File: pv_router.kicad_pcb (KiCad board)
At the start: 4 copper layers, 75 x 69.2 mm, 50 parts, among them IC1 L6981C33DR, IC2 ATM90E26-YU-B, IC3 ESP32-C3-WROOM-02-N4, J1 Barrel_Jack_Switch_Pin3Ring, J2 AudioJack3, J3 AudioJack3, J4 Barrel_Jack_Switch_Pin3Ring, J5 UART, J6 ToSSR, Q1 BSS138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

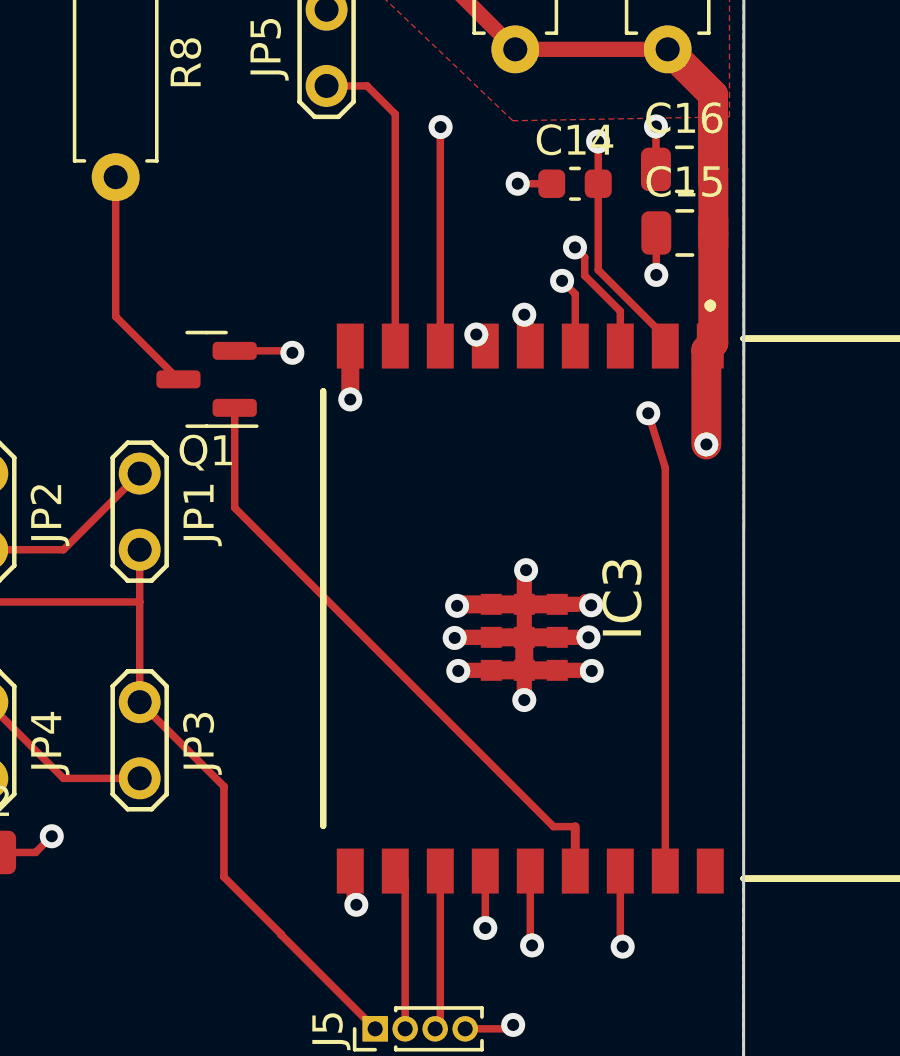
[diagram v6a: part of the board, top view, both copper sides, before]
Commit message: PCB: fix spaces between some tracks
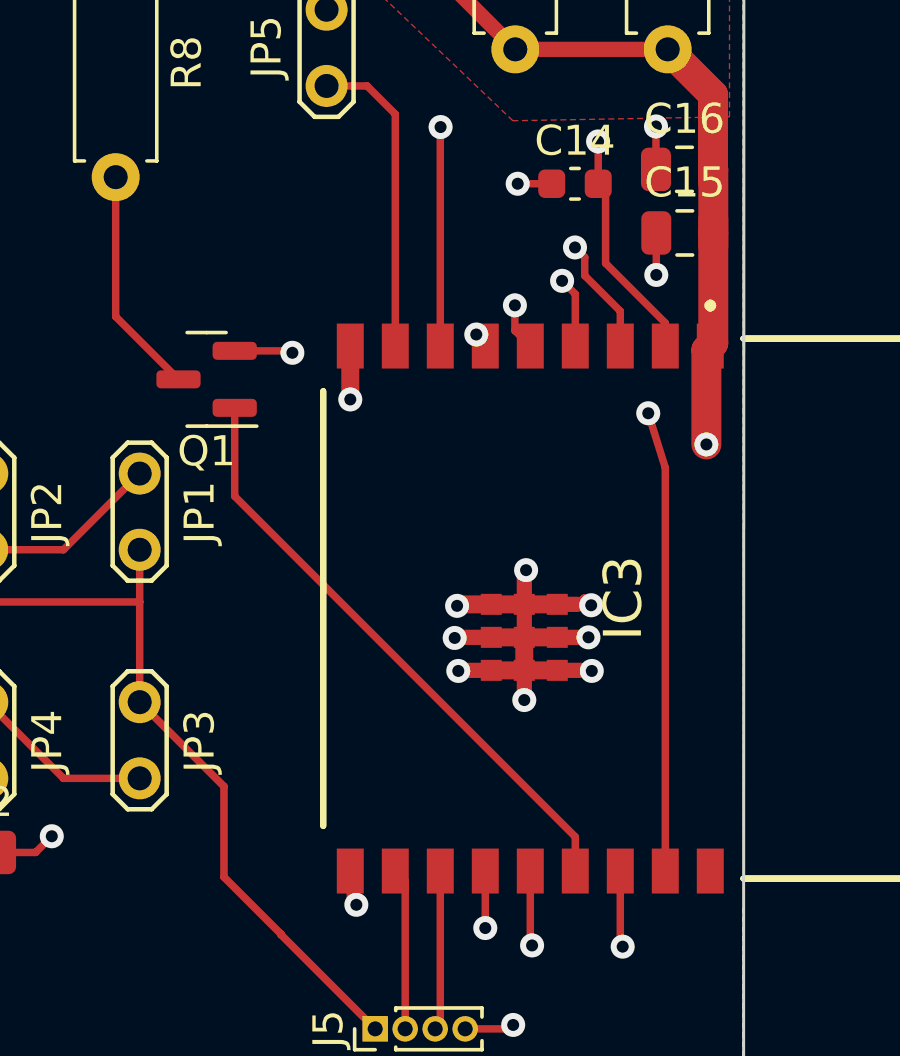
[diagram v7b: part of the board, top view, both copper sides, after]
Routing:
- net /adc/CF2: track 40.6 -> 41.4 mm
- net /adc/CF1: track 43.9 -> 44.5 mm
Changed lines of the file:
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@@
   (segment (start 164.07 140.71) (end 159.38 140.71) (width 0.25) (layer "F.Cu") (net 11))
   (segment (start 165.66 137.0321) (end 165.913264 137.285364) (width 0.3) (layer "F.Cu") (net 11))
-  (segment (start 195.155 121.555) (end 197.39 123.79) (width 0.25) (layer "F.Cu") (net 12))
-  (segment (start 195.155 118.68) (end 195.155 121.555) (width 0.25) (layer "F.Cu") (net 12))
+  (segment (start 195.4 121.33) (end 197.39 123.32) (width 0.25) (layer "F.Cu") (net 12))
   (segment (start 191.91 99.3) (end 193.12 99.3) (width 0.25) (layer "F.Cu") (net 12))
-  (segment (start 197.39 123.79) (end 197.39 124.09) (width 0.25) (layer "F.Cu") (net 12))
+  (segment (start 197.39 123.32) (end 197.39 124.09) (width 0.25) (layer "F.Cu") (net 12))
+  (segment (start 195.4 118.925) (end 195.4 121.33) (width 0.25) (layer "F.Cu") (net 12))
   (segment (start 185.11 99.3) (end 191.91 99.3) (width 0.25) (layer "F.Cu") (net 12))
   (segment (start 193.12 99.3) (end 197.48 103.66) (width 0.25) (layer "F.Cu") (net 12))
+  (segment (start 195.155 118.68) (end 195.4 118.925) (width 0.25) (layer "F.Cu") (net 12))
   (segment (start 197.48 106.57) (end 197.47 106.58) (width 0.25) (layer "F.Cu") (net 12))
   (segment (start 195.155 118.68) (end 195.155 117.275) (width 0.25) (layer "F.Cu") (net 12))
@@
   (via (at 191.09 123.705) (size 0.8) (drill 0.4) (layers "F.Cu" "B.Cu") (net 19))
   (via (at 169.01 132.35) (size 0.8) (drill 0.4) (layers "F.Cu" "B.Cu") (net 19))
-  (segment (start 169.01 132.09) (end 177.56 123.54) (width 0.25) (layer "In2.Cu") (net 19))
+  (segment (start 190.945 123.56) (end 191.09 123.705) (width 0.25) (layer "In2.Cu") (net 19))
+  (segment (start 169.01 132.09) (end 177.54 123.56) (width 0.25) (layer "In2.Cu") (net 19))
+  (segment (start 177.54 123.56) (end 190.945 123.56) (width 0.25) (layer "In2.Cu") (net 19))
   (segment (start 169.01 132.35) (end 169.01 132.09) (width 0.25) (layer "In2.Cu") (net 19))
-  (segment (start 177.56 123.54) (end 190.925 123.54) (width 0.25) (layer "In2.Cu") (net 19))
-  (segment (start 190.925 123.54) (end 191.09 123.705) (width 0.25) (layer "In2.Cu") (net 19))
-  (segment (start 192.89 123.245) (end 192.69 123.045) (width 0.25) (layer "F.Cu") (net 20))
+  (segment (start 192.3775 123.5775) (end 192.3775 122.7325) (width 0.25) (layer "F.Cu") (net 20))
   (segment (start 167.61 135.96) (end 167.61 134.400756) (width 0.25) (layer "F.Cu") (net 20))
-  (segment (start 192.89 124.09) (end 192.89 123.245) (width 0.25) (layer "F.Cu") (net 20))
+  (segment (start 192.89 124.09) (end 192.3775 123.5775) (width 0.25) (layer "F.Cu") (net 20))
   (segment (start 167.61 134.400756) (end 167.091412 133.882168) (width 0.25) (layer "F.Cu") (net 20))
-  (via (at 192.69 123.045) (size 0.8) (drill 0.4) (layers "F.Cu" "B.Cu") (net 20))
+  (via (at 192.3775 122.7325) (size 0.8) (drill 0.4) (layers "F.Cu" "B.Cu") (net 20))
   (via (at 167.091412 133.882168) (size 0.8) (drill 0.4) (layers "F.Cu" "B.Cu") (net 20))
-  (segment (start 167.091412 132.852309) (end 177.013721 122.93) (width 0.25) (layer "In2.Cu") (net 20))
+  (segment (start 177.211221 122.7325) (end 192.3775 122.7325) (width 0.25) (layer "In2.Cu") (net 20))
+  (segment (start 167.091412 132.852309) (end 177.211221 122.7325) (width 0.25) (layer "In2.Cu") (net 20))
   (segment (start 167.091412 133.882168) (end 167.091412 132.852309) (width 0.25) (layer "In2.Cu") (net 20))
-  (segment (start 192.575 122.93) (end 192.69 123.045) (width 0.25) (layer "In2.Cu") (net 20))
-  (segment (start 177.013721 122.93) (end 192.575 122.93) (width 0.25) (layer "In2.Cu") (net 20))
   (segment (start 186.89 142.512829) (end 187.092171 142.715) (width 0.25) (layer "F.Cu") (net 21))
   (segment (start 165.01 137.513471) (end 165.113264 137.616735) (width 0.25) (layer "F.Cu") (net 21))
@@
   (via (at 163.69995 133.64995) (size 0.8) (drill 0.4) (layers "F.Cu" "B.Cu") (net 23))
   (via (at 193.94999 121.916283) (size 0.8) (drill 0.4) (layers "F.Cu" "B.Cu") (net 23))
+  (segment (start 192.833707 120.8) (end 193.94999 121.916283) (width 0.25) (layer "In2.Cu") (net 23))
+  (segment (start 167.085 130.791016) (end 167.085 129.615) (width 0.25) (layer "In2.Cu") (net 23))
+  (segment (start 167.085 129.615) (end 175.9 120.8) (width 0.25) (layer "In2.Cu") (net 23))
+  (segment (start 163.69995 133.64995) (end 164.226066 133.64995) (width 0.25) (layer "In2.Cu") (net 23))
   (segment (start 164.226066 133.64995) (end 167.085 130.791016) (width 0.25) (layer "In2.Cu") (net 23))
-  (segment (start 175.225392 121.664888) (end 193.698595 121.664888) (width 0.25) (layer "In2.Cu") (net 23))
-  (segment (start 167.085 130.791016) (end 167.085 129.80528) (width 0.25) (layer "In2.Cu") (net 23))
-  (segment (start 167.085 129.80528) (end 175.225392 121.664888) (width 0.25) (layer "In2.Cu") (net 23))
-  (segment (start 163.69995 133.64995) (end 164.226066 133.64995) (width 0.25) (layer "In2.Cu") (net 23))
-  (segment (start 193.698595 121.664888) (end 193.94999 121.916283) (width 0.25) (layer "In2.Cu") (net 23))
+  (segment (start 175.9 120.8) (end 192.833707 120.8) (width 0.25) (layer "In2.Cu") (net 23))
   (segment (start 195.89 124.09) (end 195.89 122.926396) (width 0.25) (layer "F.Cu") (net 24))
   (segment (start 163.06 134.574858) (end 162.52001 134.034868) (width 0.25) (layer "F.Cu") (net 24))
@@
   (via (at 194.380046 120.80346) (size 0.8) (drill 0.4) (layers "F.Cu" "B.Cu") (net 24))
   (via (at 162.52001 134.034868) (size 0.8) (drill 0.4) (layers "F.Cu" "B.Cu") (net 24))
+  (segment (start 175.613984 120.07) (end 193.646586 120.07) (width 0.25) (layer "In2.Cu") (net 24))
+  (segment (start 162.52001 134.034868) (end 162.52001 133.733874) (width 0.25) (layer "In2.Cu") (net 24))
+  (segment (start 193.646586 120.07) (end 194.380046 120.80346) (width 0.25) (layer "In2.Cu") (net 24))
+  (segment (start 162.52001 133.733874) (end 165.535 130.718884) (width 0.25) (layer "In2.Cu") (net 24))
   (segment (start 165.535 130.718884) (end 165.535 130.148984) (width 0.25) (layer "In2.Cu") (net 24))
-  (segment (start 165.535 130.148984) (end 174.880524 120.80346) (width 0.25) (layer "In2.Cu") (net 24))
-  (segment (start 162.52001 133.733874) (end 165.535 130.718884) (width 0.25) (layer "In2.Cu") (net 24))
-  (segment (start 174.880524 120.80346) (end 194.380046 120.80346) (width 0.25) (layer "In2.Cu") (net 24))
-  (segment (start 162.52001 134.034868) (end 162.52001 133.733874) (width 0.25) (layer "In2.Cu") (net 24))
+  (segment (start 165.535 130.148984) (end 175.613984 120.07) (width 0.25) (layer "In2.Cu") (net 24))
   (segment (start 192.89 144.01) (end 192.89 141.59) (width 0.25) (layer "F.Cu") (net 25))
   (segment (start 162.41 136.94) (end 161.62 137.73) (width 0.25) (layer "F.Cu") (net 25))
@@
   (via (at 167.824357 131.023348) (size 0.8) (drill 0.4) (layers "F.Cu" "B.Cu") (net 26))
   (segment (start 167.824357 129.945643) (end 167.824357 131.023348) (width 0.25) (layer "In2.Cu") (net 26))
-  (segment (start 196.8219 125.884209) (end 193.257691 122.32) (width 0.25) (layer "In2.Cu") (net 26))
+  (segment (start 192.687691 121.75) (end 176.02 121.75) (width 0.25) (layer "In2.Cu") (net 26))
   (segment (start 196.8219 126.33) (end 196.8219 125.884209) (width 0.25) (layer "In2.Cu") (net 26))
-  (segment (start 175.45 122.32) (end 167.824357 129.945643) (width 0.25) (layer "In2.Cu") (net 26))
-  (segment (start 193.257691 122.32) (end 175.45 122.32) (width 0.25) (layer "In2.Cu") (net 26))
+  (segment (start 196.8219 125.884209) (end 192.687691 121.75) (width 0.25) (layer "In2.Cu") (net 26))
+  (segment (start 176.02 121.75) (end 167.824357 129.945643) (width 0.25) (layer "In2.Cu") (net 26))
   (segment (start 174.79 130.88) (end 177.33 130.88) (width 0.25) (layer "F.Cu") (net 27))
   (segment (start 177.33 130.88) (end 179.87 128.34) (width 0.25) (layer "F.Cu") (net 27))
@@
   (segment (start 169.56 128.964) (end 169.56 130.4301) (width 0.25) (layer "F.Cu") (net 27))
   (segment (start 169.56 130.4301) (end 174.3401 130.4301) (width 0.25) (layer "F.Cu") (net 27))
-  (segment (start 183.0375 126.15) (end 183.0375 129.483516) (width 0.25) (layer "F.Cu") (net 29))
-  (segment (start 183.0375 129.483516) (end 193.663984 140.11) (width 0.25) (layer "F.Cu") (net 29))
-  (segment (start 194.39 141.59) (end 194.39 140.11) (width 0.3) (layer "F.Cu") (net 29))
-  (segment (start 193.663984 140.11) (end 194.39 140.11) (width 0.25) (layer "F.Cu") (net 29))
+  (segment (start 183.0375 129.0975) (end 183.0375 126.15) (width 0.25) (layer "F.Cu") (net 29))
+  (segment (start 194.39 140.45) (end 183.0375 129.0975) (width 0.25) (layer "F.Cu") (net 29))
+  (segment (start 194.39 141.59) (end 194.39 140.45) (width 0.25) (layer "F.Cu") (net 29))
   (segment (start 189.89 146.68) (end 189.72 146.85) (width 0.25) (layer "F.Cu") (net 30))
   (segment (start 189.89 141.59) (end 189.89 146.68) (width 0.25) (layer "F.Cu") (net 30))

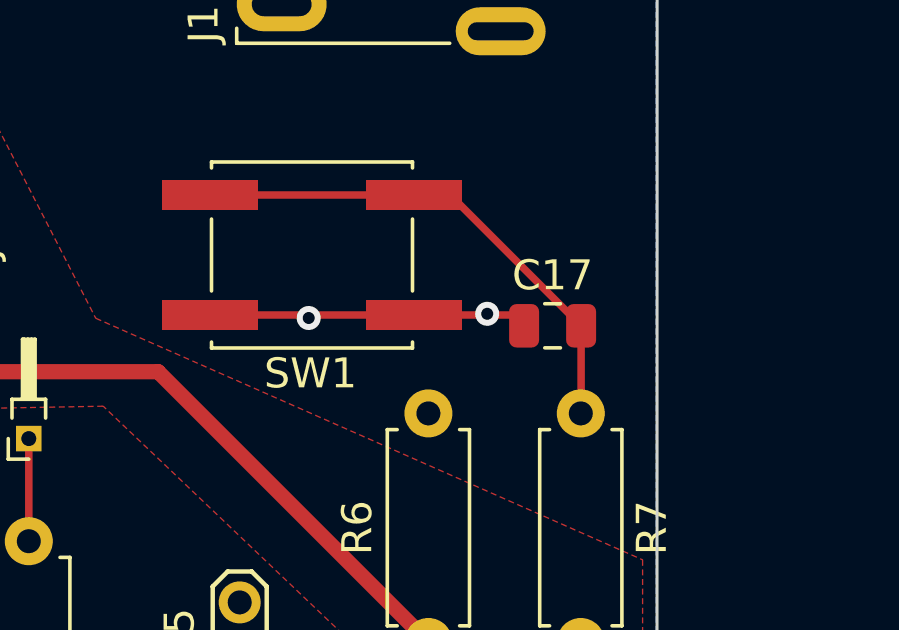
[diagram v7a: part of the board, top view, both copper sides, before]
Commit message: PCB: fix button GND track
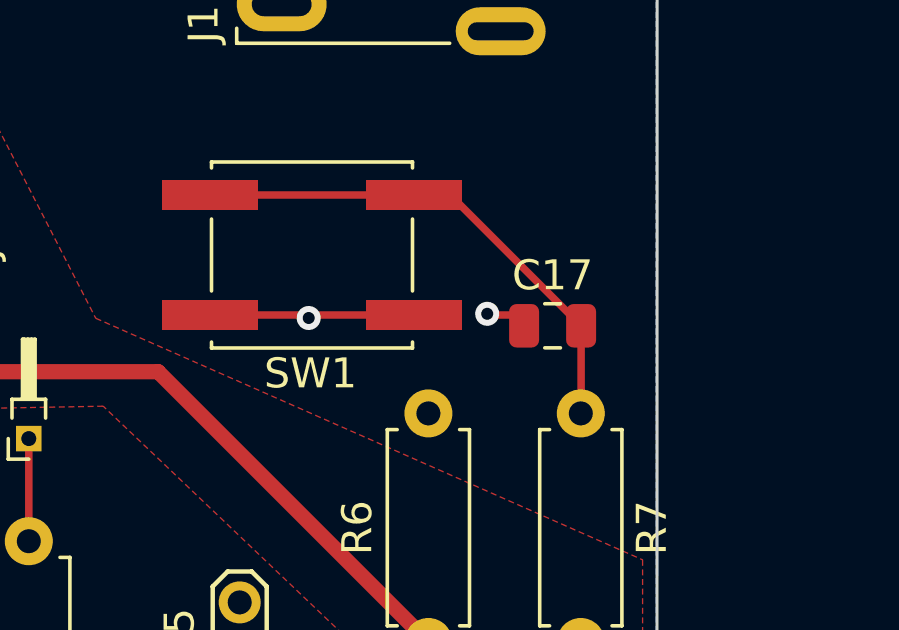
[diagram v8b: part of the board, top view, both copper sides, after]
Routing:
- net GND: track 77.3 -> 74.9 mm
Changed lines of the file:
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@@
   (segment (start 153.39 139.35) (end 153.45 139.29) (width 0.25) (layer "F.Cu") (net 2))
   (segment (start 166.31 128.964) (end 166.31 130.47) (width 0.25) (layer "F.Cu") (net 2))
-  (segment (start 191.91 103.3) (end 194.31 103.3) (width 0.25) (layer "F.Cu") (net 2))
   (segment (start 160.344 128.964) (end 160.34 128.96) (width 0.25) (layer "F.Cu") (net 2))
   (segment (start 185.11 103.3) (end 188.3 103.3) (width 0.25) (layer "F.Cu") (net 2))
